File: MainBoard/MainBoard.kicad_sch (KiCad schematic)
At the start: 42 parts, among them U1 TL074CN, U2 TL074CN, U3 TL074CN

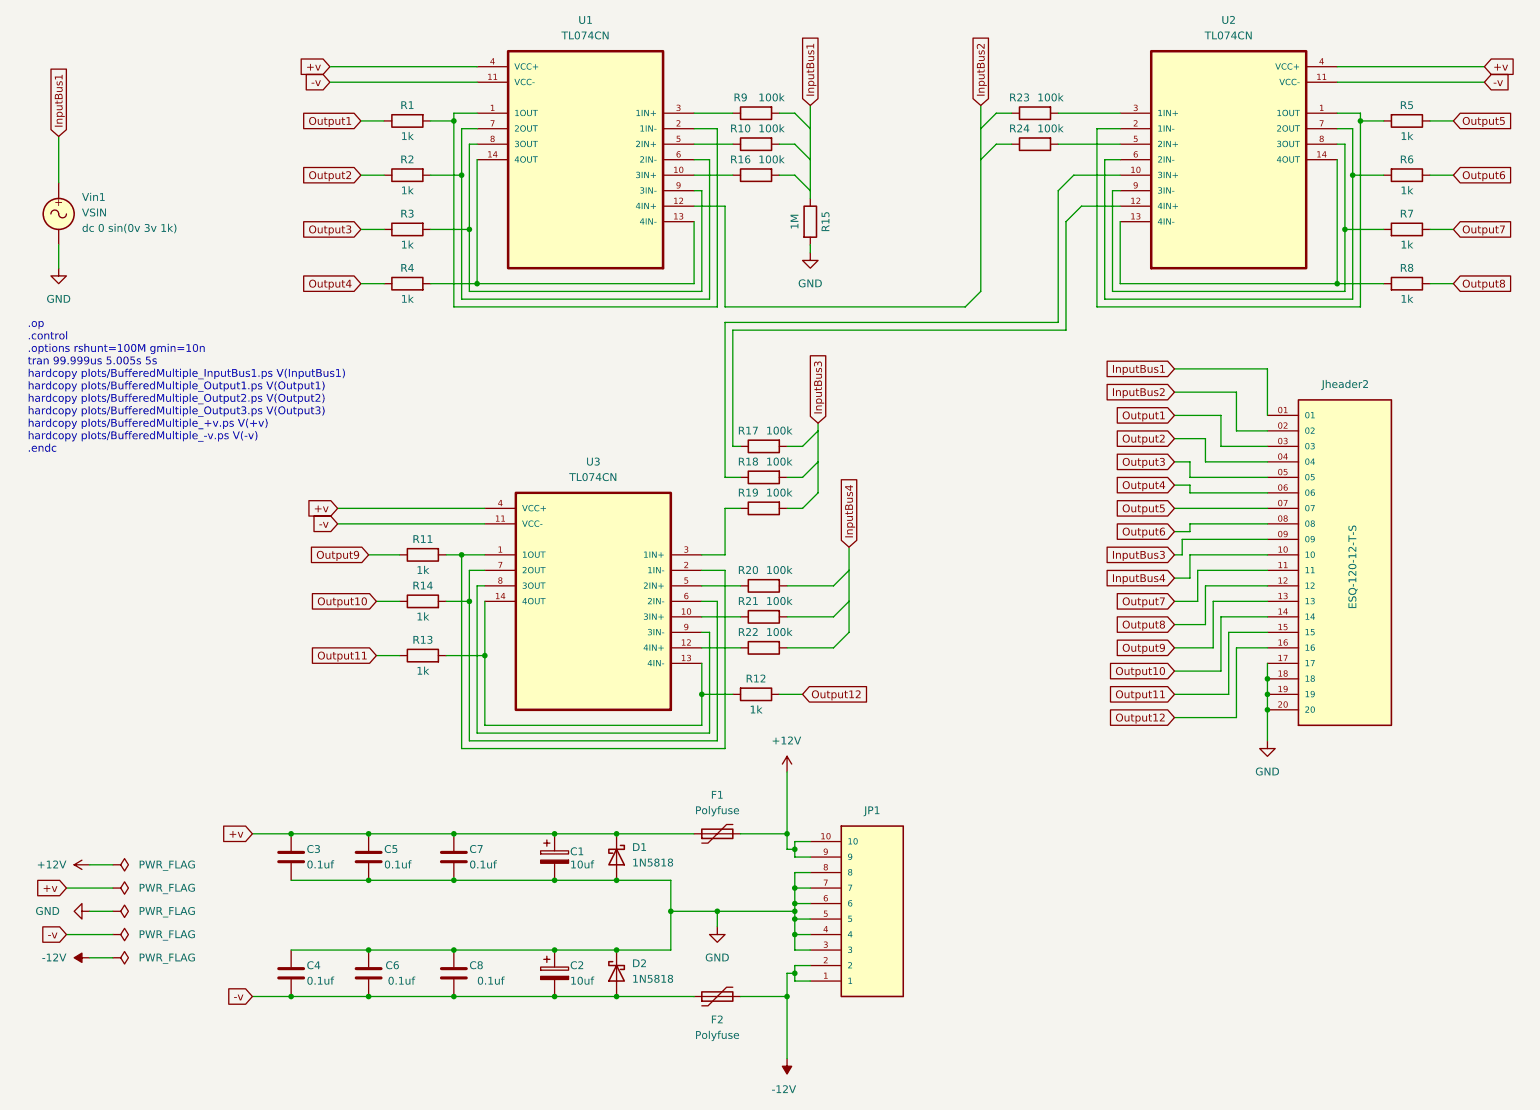
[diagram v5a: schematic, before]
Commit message: updated power supply
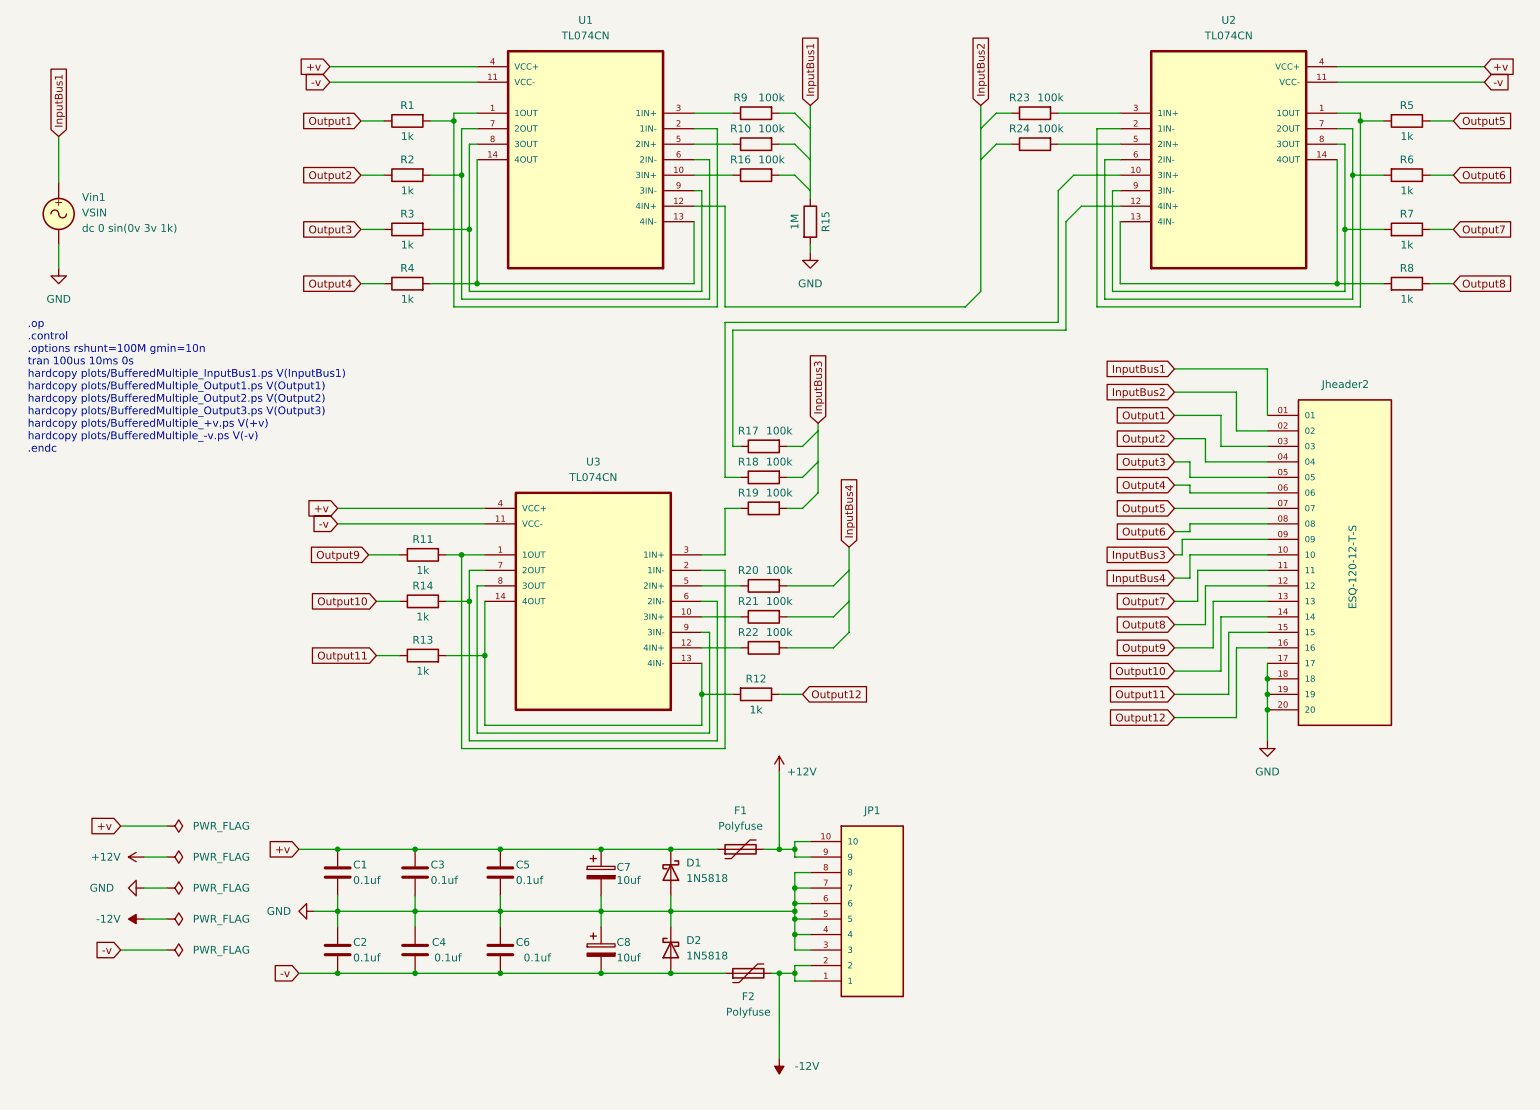
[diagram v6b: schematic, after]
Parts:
- removed C1, C2: 10uf, Capacitor_THT:CP_Radial_D5.0mm_P2.50mm, symbol Device:C_Polarized
- removed C7, C8: 0.1uf, Capacitor_THT:C_Radial_D4.0mm_H5.0mm_P1.50mm, symbol Device:C
- added C1: 0.1uf, 1-146763-5:TE_1-146763-5, symbol Device:C
- added C2: 0.1uf, Capacitor_THT:C_Radial_D4.0mm_H5.0mm_P1.50mm, symbol Device:C
- added C7, C8: 10uf, Capacitor_THT:CP_Radial_D5.0mm_P2.50mm, symbol Device:C_Polarized
- JP1: footprint TE_1761681-3 -> 1761681-3:TE_1761681-3
- Jheader2: footprint SAMTEC_ESQ-120-12-T-S -> ESQ-120-12-T-S:SAMTEC_ESQ-120-12-T-S
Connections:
- net +v: now also C1.1, C7.1
- net -v: now also C2.1, C8.2
- net GND: now also C1.2, C2.2, C7.2, C8.1
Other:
- note added: ".op .control .options rshunt=100M gmin=10n tran 100us 10ms 0s hardcopy plots/BufferedMultiple_InputBus1.ps V(InputBus1) hardcopy plots/BufferedMultiple_Output1.ps V(Output1) hardcopy plots/BufferedMultiple_Output2.ps V(Output2) hardcopy plots/BufferedMultiple_Output3.ps V(Output3) hardcopy plots/BufferedMultiple_+v.ps V(+v) hardcopy plots/BufferedMultiple_-v.ps V(-v) .endc"
- note removed: ".op .control .options rshunt=100M gmin=10n tran 99.999us 5.005s 5s hardcopy plots/BufferedMultiple_InputBus1.ps V(InputBus1) hardcopy plots/BufferedMultiple_Output1.ps V(Output1) hardcopy plots/BufferedMultiple_Output2.ps V(Output2) hardcopy plots/BufferedMultiple_Output3.ps V(Output3) hardcopy plots/BufferedMultiple_+v.ps V(+v) hardcopy plots/BufferedMultiple_-v.ps V(-v) .endc"
- moved on the sheet: F1, F2

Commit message: remove simulation.  added project level symbols and footprints
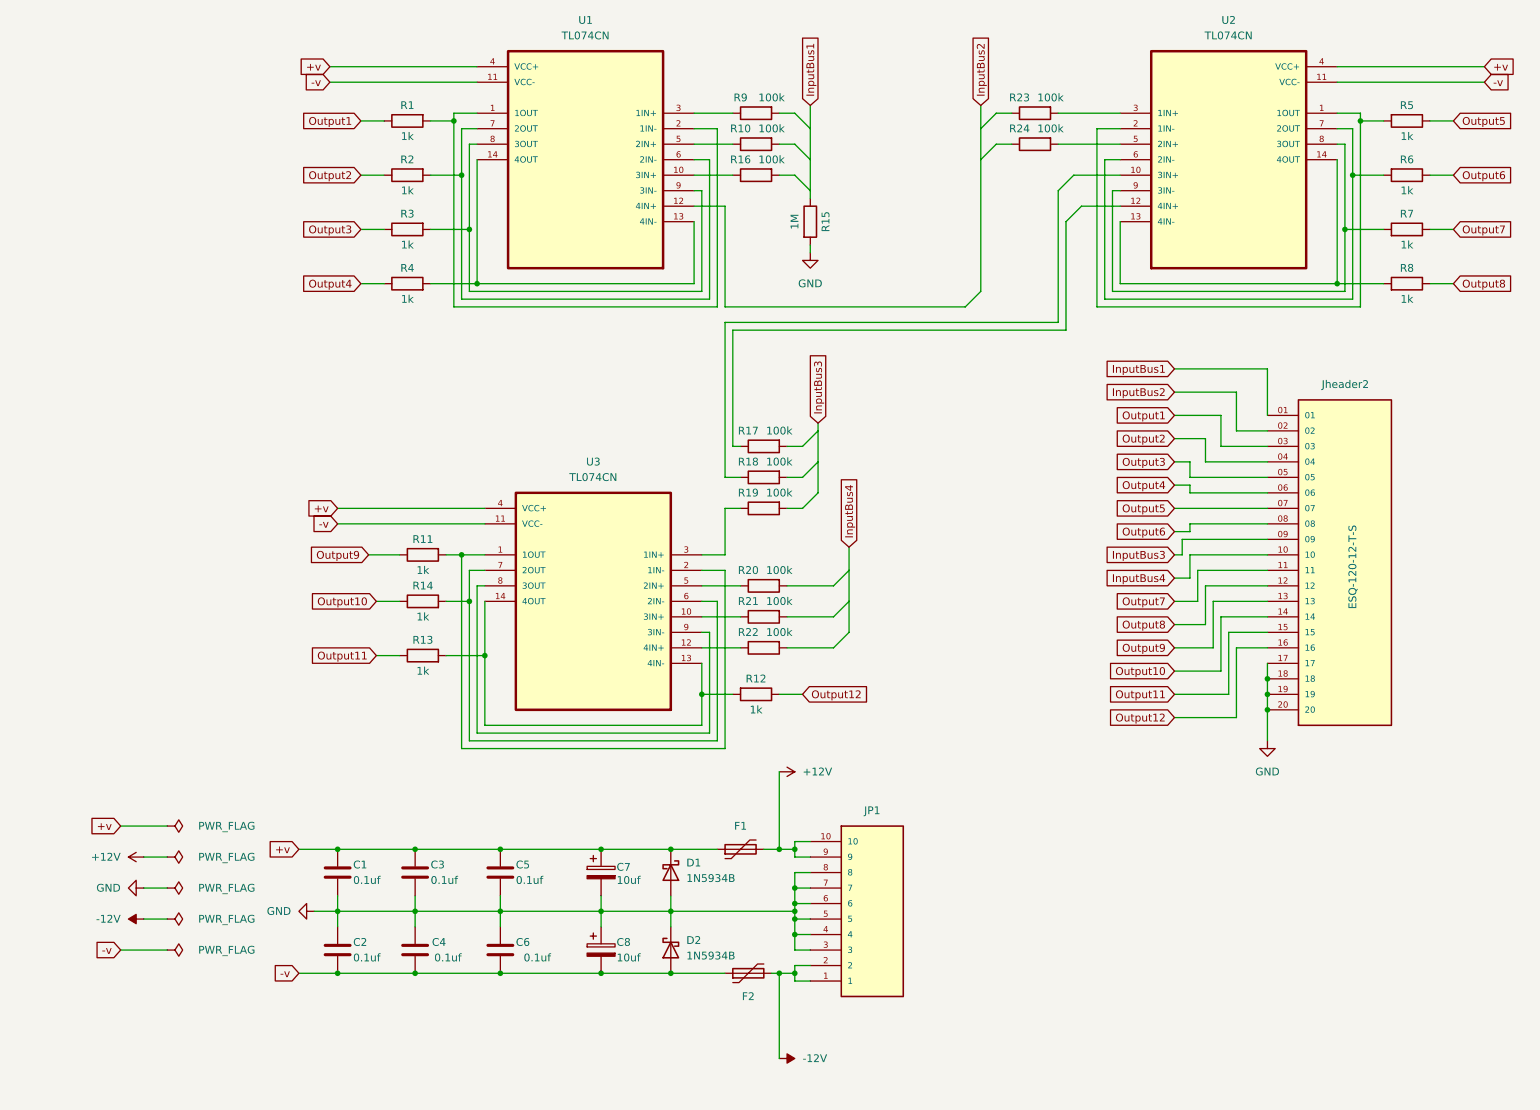
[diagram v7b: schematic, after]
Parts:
- removed Vin1: VSIN, symbol Simulation_SPICE:VSIN
- C1: footprint 1-146763-5:TE_1-146763-5 -> Capacitor_THT:C_Radial_D4.0mm_H5.0mm_P1.50mm
- D1, D2: value 1N5818 -> 1N5934B; footprint Diode_THT:D_DO-41_SOD81_P10.16mm_Horizontal -> 1N5934B:P2_DO-201; Spice_Lib_File ../models/1N5818.mod -> (none); Spice_Model 1N5818 -> (none); Spice_Netlist_Enabled Y -> (none); Spice_Primitive D -> (none)
- F1, F2: value Polyfuse -> ${SIM.PARAMS}; Spice_Netlist_Enabled N -> (none); Spice_Primitive R -> (none)
- JP1: Spice_Model 1761681-3 -> (none); Spice_Netlist_Enabled N -> (none); Spice_Primitive J -> (none)
- Jheader2: Spice_Model ESQ-120-12-T-S -> (none); Spice_Netlist_Enabled N -> (none); Spice_Primitive J -> (none)
- R1, R10, R11, R12, R13, R14, R15, R16, R17, R18, R19, R2, R20, R21, R22, R23, R24, R3, R4, R5, R6, R7, R8, R9: footprint Resistor_THT:R_Axial_DIN0204_L3.6mm_D1.6mm_P2.54mm_Vertical -> Resistor_THT:R_Axial_DIN0204_L3.6mm_D1.6mm_P5.08mm_Horizontal
- U1, U2, U3: Spice_Lib_File ../models/TL074.mod -> (none); Spice_Model TL074 -> (none); Spice_Netlist_Enabled Y -> (none); Spice_Primitive X -> (none)
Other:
- note removed: ".op .control .options rshunt=100M gmin=10n tran 100us 10ms 0s hardcopy plots/BufferedMultiple_InputBus1.ps V(InputBus1) hardcopy plots/BufferedMultiple_Output1.ps V(Output1) hardcopy plots/BufferedMultiple_Output2.ps V(Output2) hardcopy plots/BufferedMultiple_Output3.ps V(Output3) hardcopy plots/BufferedMultiple_+v.ps V(+v) hardcopy plots/BufferedMultiple_-v.ps V(-v) .endc"

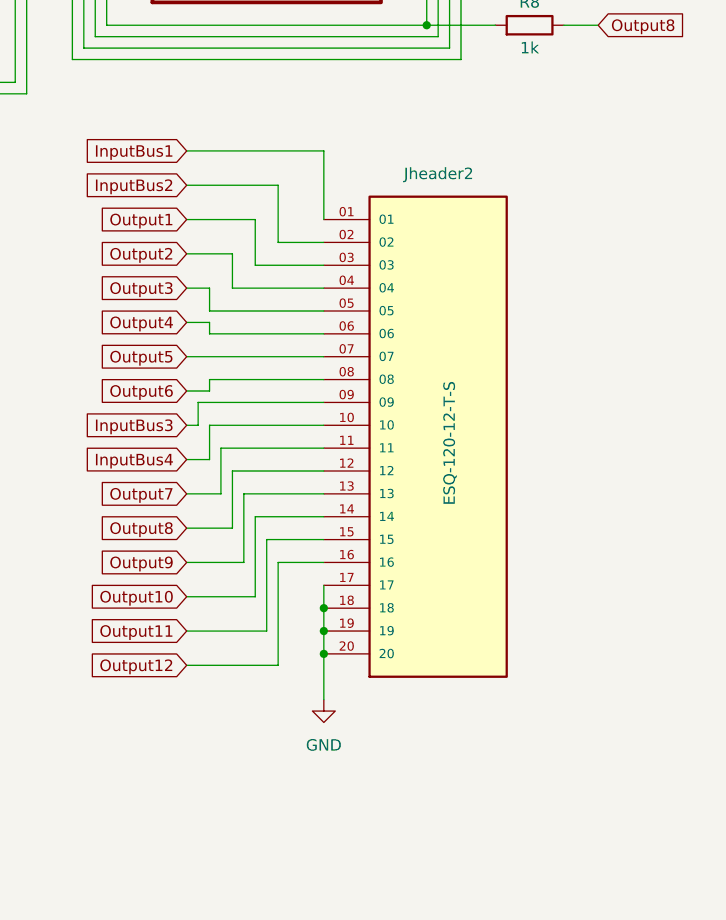
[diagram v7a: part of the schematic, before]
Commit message: updated with new footprints and 3d models
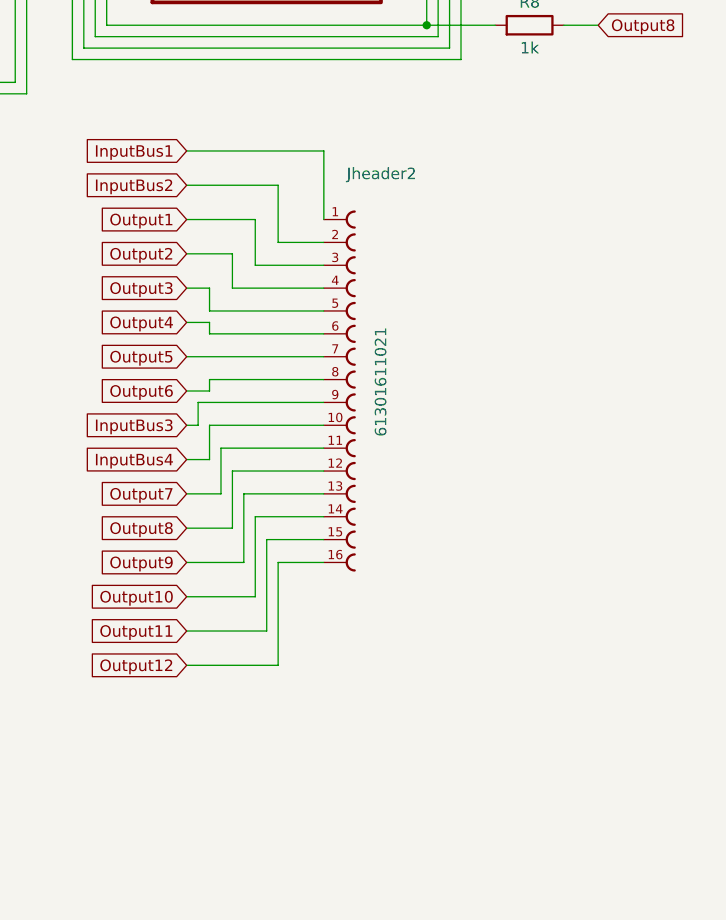
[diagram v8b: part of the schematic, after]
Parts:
- C1, C2, C3, C4, C5, C6: footprint Capacitor_THT:C_Radial_D4.0mm_H5.0mm_P1.50mm -> Capacitor_THT:C_Disc_D7.5mm_W4.4mm_P5.00mm
- Jheader2: value ESQ-120-12-T-S -> 61301611021; footprint ESQ-120-12-T-S:SAMTEC_ESQ-120-12-T-S -> 61301611021:61301611021; symbol ESQ-120-12-T-S:ESQ-120-12-T-S -> 61301611021:61301611021; Centerline_Pitch (none) -> 2.54 mm[.1 in]; Comment (none) -> 1-826936-6; EU_RoHS_Compliance (none) -> Compliant; Number_of_Positions (none) -> 16; Product_Type (none) -> Connector
- R1, R10, R11, R12, R13, R14, R15, R16, R17, R18, R19, R2, R20, R21, R22, R23, R24, R3, R4, R5, R6, R7, R8, R9: footprint Resistor_THT:R_Axial_DIN0204_L3.6mm_D1.6mm_P5.08mm_Horizontal -> Resistor_THT:R_Axial_DIN0207_L6.3mm_D2.5mm_P10.16mm_Horizontal
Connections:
- net GND: no longer Jheader2.17, Jheader2.18, Jheader2.19, Jheader2.20
- net InputBus1: now also Jheader2.1; no longer Jheader2.01
- net InputBus2: now also Jheader2.2; no longer Jheader2.02
- net InputBus3: now also Jheader2.9; no longer Jheader2.09
- net Output1: now also Jheader2.3; no longer Jheader2.03
- net Output2: now also Jheader2.4; no longer Jheader2.04
- net Output3: now also Jheader2.5; no longer Jheader2.05
- net Output4: now also Jheader2.6; no longer Jheader2.06
- net Output5: now also Jheader2.7; no longer Jheader2.07
- net Output6: now also Jheader2.8; no longer Jheader2.08
